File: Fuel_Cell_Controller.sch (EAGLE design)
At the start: 27 parts, among them U1 MAX232PTH

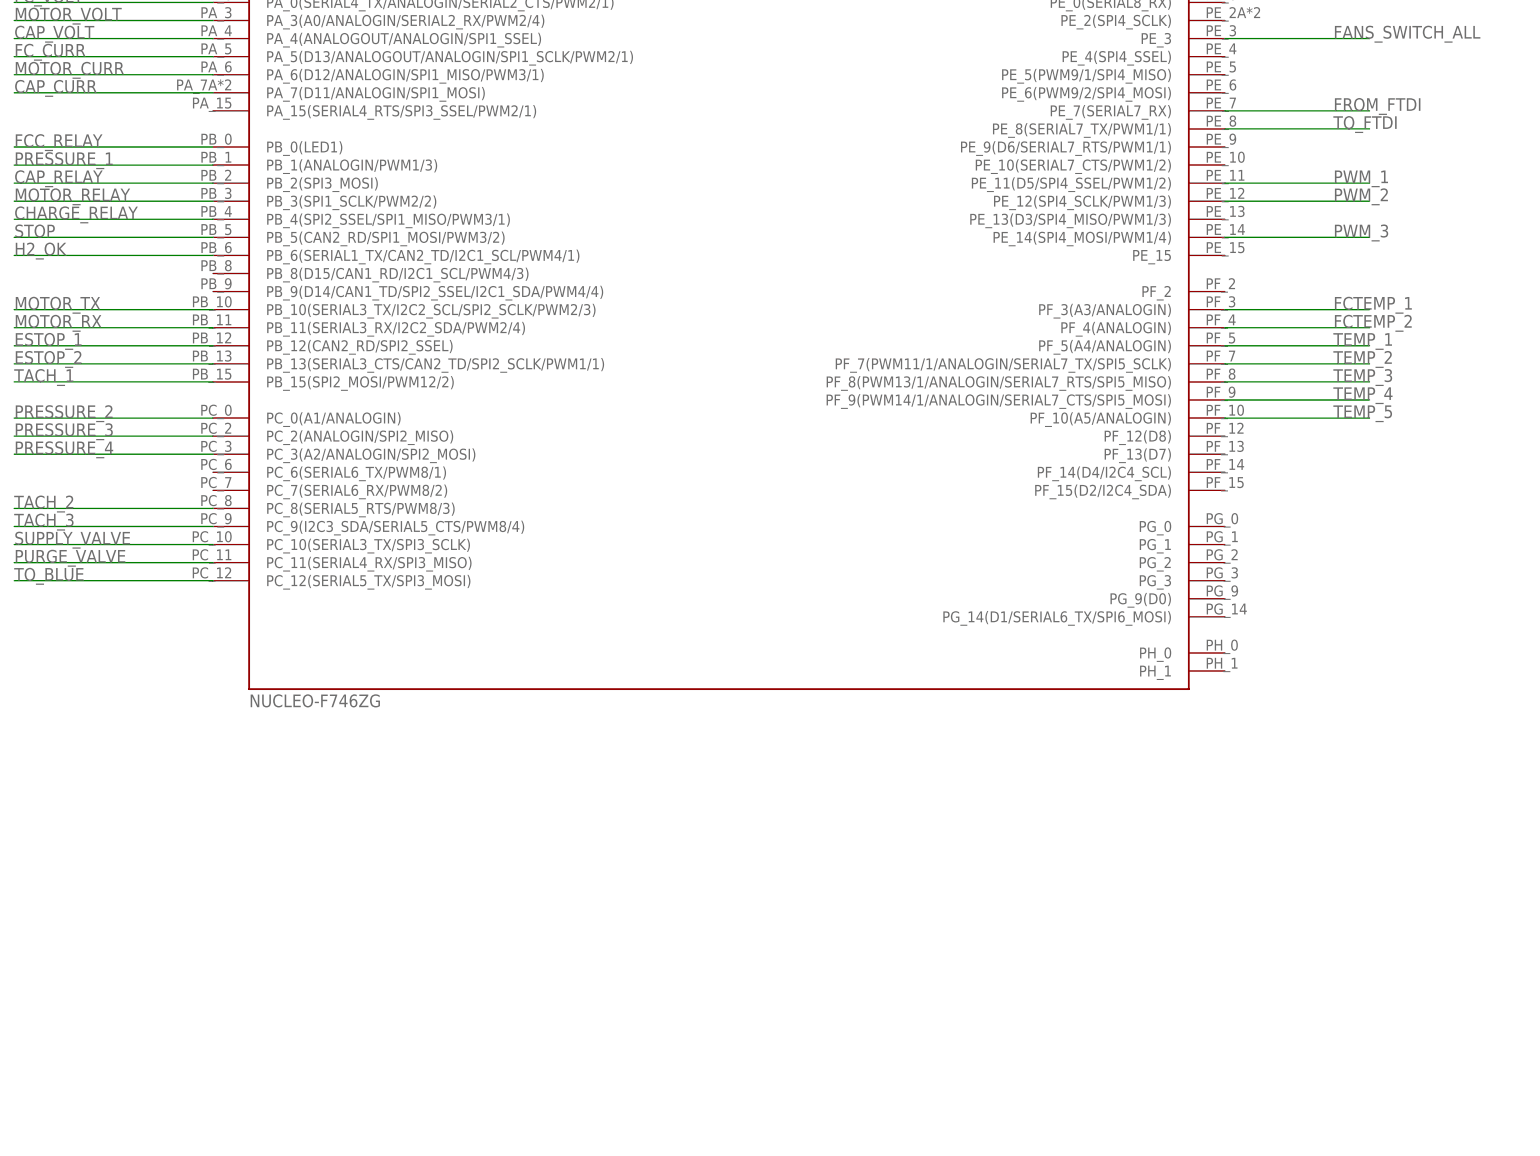
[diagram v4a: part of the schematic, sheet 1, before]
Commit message: added some buffers
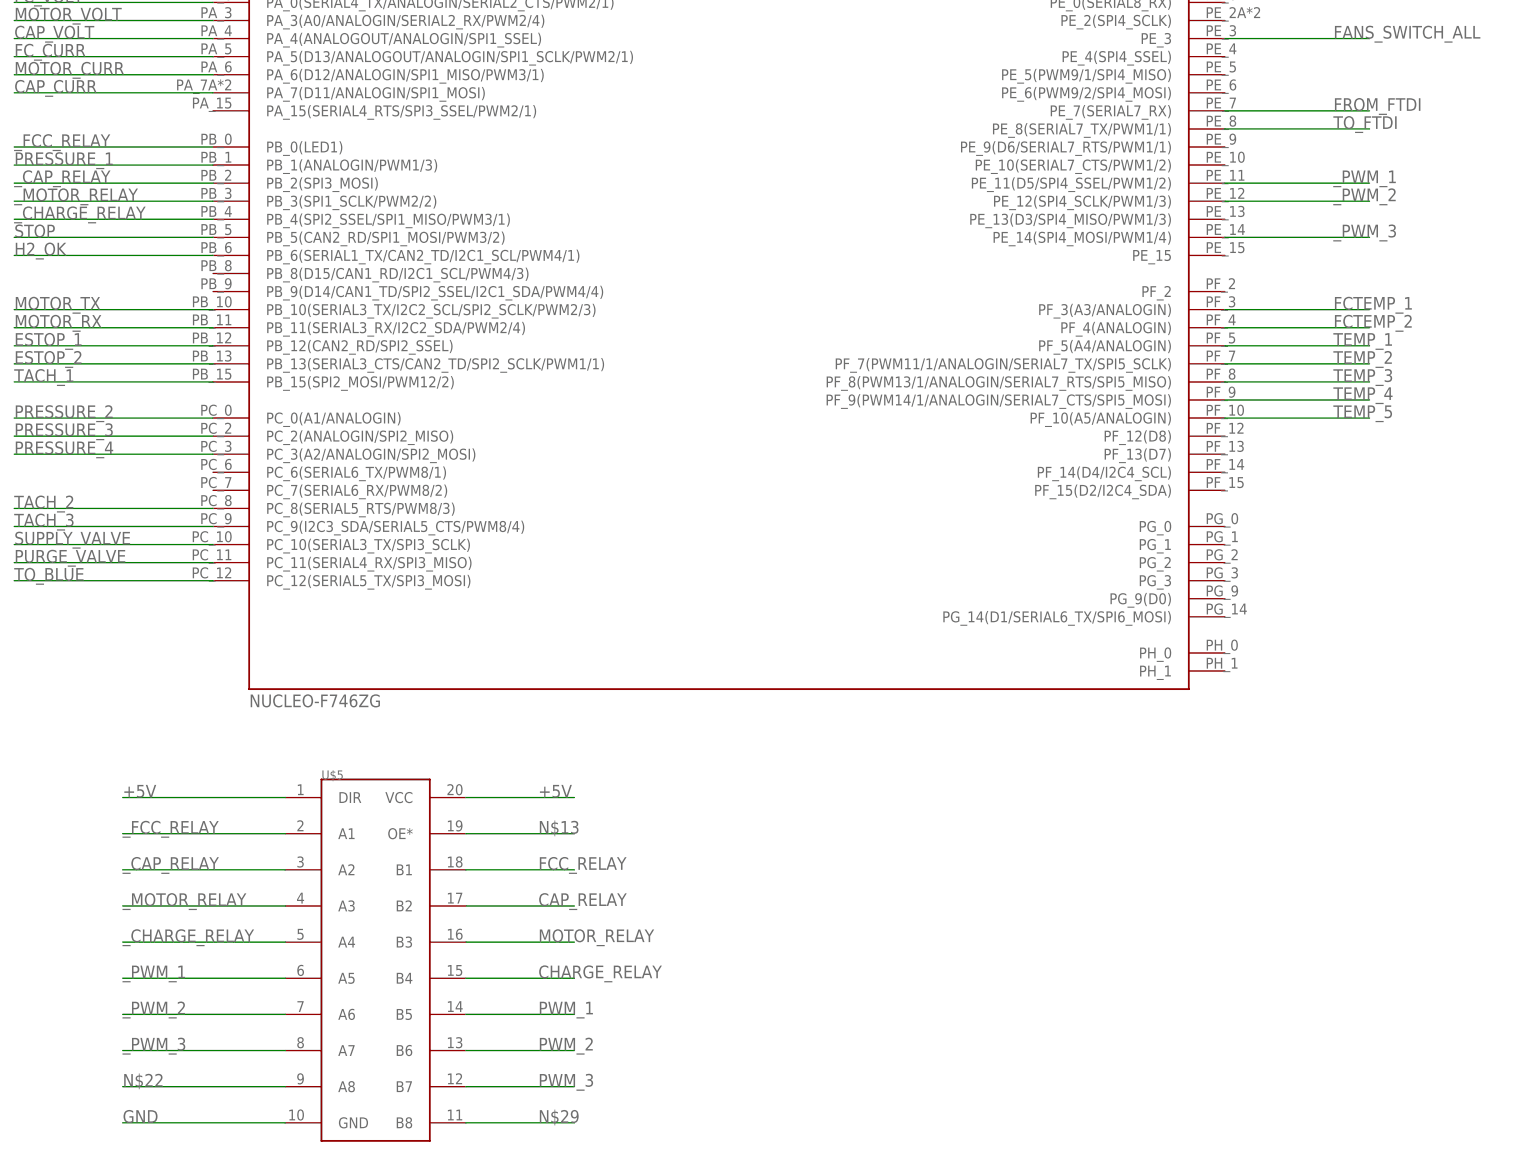
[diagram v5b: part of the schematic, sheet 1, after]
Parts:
- added U$5: SN74LVC245AN, FCC_parts:SN74LVC245AN
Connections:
- new net N$13: U$5.OE*
- new net N$22: U$5.A8
- new net N$29: U$5.B8
- new net _CAP_RELAY: U$1.PB_2(SPI3_MOSI), U$5.A2
- new net _CHARGE_RELAY: U$1.PB_4(SPI2_SSEL/SPI1_MISO/PWM3/1), U$5.A4
- new net _FCC_RELAY: U$1.PB_0(LED1), U$5.A1
- new net _MOTOR_RELAY: U$1.PB_3(SPI1_SCLK/PWM2/2), U$5.A3
- new net _PWM_1: U$1.PE_11(D5/SPI4_SSEL/PWM1/2), U$5.A5
- new net _PWM_2: U$1.PE_12(SPI4_SCLK/PWM1/3), U$5.A6
- new net _PWM_3: U$1.PE_14(SPI4_MOSI/PWM1/4), U$5.A7
- net +5V: now also U$5.DIR, U$5.VCC
- net CAP_RELAY: now also U$5.B2; no longer U$1.PB_2(SPI3_MOSI)
- net CHARGE_RELAY: now also U$5.B4; no longer U$1.PB_4(SPI2_SSEL/SPI1_MISO/PWM3/1)
- net FCC_RELAY: now also U$5.B1; no longer U$1.PB_0(LED1)
- net GND: now also U$5.GND
- net MOTOR_RELAY: now also U$5.B3; no longer U$1.PB_3(SPI1_SCLK/PWM2/2)
- net PWM_1: now also U$5.B5; no longer U$1.PE_11(D5/SPI4_SSEL/PWM1/2)
- net PWM_2: now also U$5.B6; no longer U$1.PE_12(SPI4_SCLK/PWM1/3)
- net PWM_3: now also U$5.B7; no longer U$1.PE_14(SPI4_MOSI/PWM1/4)

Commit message: buffer changes
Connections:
- removed net N$13: U$5.OE*
- removed net N$22: U$5.A8
- removed net N$29: U$5.B8
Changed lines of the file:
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@@
-</segment>
-</net>
-<net name="N$13" class="0">
-<segment>
-<pinref part="U$5" gate="G$1" pin="OE*"/>
-<wire x1="-35.56" y1="-88.9" x2="-20.32" y2="-88.9" width="0.1524" layer="91"/>
-<label x="-25.4" y="-88.9" size="1.778" layer="95"/>
 </segment>
 </net>
@@
 <wire x1="-35.56" y1="-93.98" x2="-20.32" y2="-93.98" width="0.1524" layer="91"/>
 <label x="-25.4" y="-93.98" size="1.778" layer="95"/>
-</segment>
-</net>
-<net name="N$22" class="0">
-<segment>
-<pinref part="U$5" gate="G$1" pin="A8"/>
-<wire x1="-60.96" y1="-124.46" x2="-83.82" y2="-124.46" width="0.1524" layer="91"/>
-<label x="-83.82" y="-124.46" size="1.778" layer="95"/>
 </segment>
 </net>
@@
 </segment>
 </net>
-<net name="N$29" class="0">
-<segment>
-<pinref part="U$5" gate="G$1" pin="B8"/>
-<wire x1="-35.56" y1="-129.54" x2="-20.32" y2="-129.54" width="0.1524" layer="91"/>
-<label x="-25.4" y="-129.54" size="1.778" layer="95"/>
-</segment>
-</net>

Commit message: Added humidity sensor
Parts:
- added JP1: (no value), jumper:JP2E
- added SHTSENSOR: SHT31-DIS, FCC_parts:SHT31-DIS
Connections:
- new net HUMID_RESET: U$1.PC_6(SERIAL6_TX/PWM8/1)
- new net HUMID_RST: SHTSENSOR.RST
- new net I2C1_SCL: U$1.PB_8(D15/CAN1_RD/I2C1_SCL/PWM4/3)
- new net ISC1_SCL: SHTSENSOR.SCL
- new net ISC1_SDA: SHTSENSOR.SDA, U$1.PB_9(D14/CAN1_TD/SPI2_SSEL/I2C1_SDA/PWM4/4)
- new net SHT_ADR: JP1.2, SHTSENSOR.ADR
- net +5V: now also JP1.3, SHTSENSOR.VIN
- net GND: now also JP1.1, SHTSENSOR.GND
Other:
- note added: "TEMP/HUMID SENSOR"
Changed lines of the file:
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@@
 <part name="U$10" library="FCC_parts" deviceset="UMFT234XF" device="UMFT234XF"/>
 <part name="U$5" library="FCC_parts" deviceset="SN74LVC245AN" device=""/>
+<part name="SHTSENSOR" library="FCC_parts" deviceset="SHT31-DIS" device=""/>
+<part name="JP1" library="jumper" library_urn="urn:adsk.eagle:library:252" deviceset="JP2E" device="" package3d_urn="urn:adsk.eagle:package:15452/1"/>
 </parts>
 <sheets>
@@
 <wire x1="281.94" y1="33.02" x2="281.94" y2="-15.24" width="0.1524" layer="94"/>
 <wire x1="281.94" y1="-15.24" x2="210.82" y2="-15.24" width="0.1524" layer="94"/>
+<text x="228.6" y="-25.4" size="3.81" layer="94">TEMP/HUMID SENSOR</text>
+<wire x1="210.82" y1="-96.52" x2="304.8" y2="-96.52" width="0.1524" layer="94"/>
+<wire x1="304.8" y1="-96.52" x2="304.8" y2="-15.24" width="0.1524" layer="94"/>
+<wire x1="304.8" y1="-15.24" x2="281.94" y2="-15.24" width="0.1524" layer="94"/>
 </plain>
 <instances>
@@
 <instance part="U$10" gate="G$1" x="220.98" y="53.34"/>
 <instance part="U$5" gate="G$1" x="-48.26" y="-106.68"/>
+<instance part="SHTSENSOR" gate="G$1" x="266.7" y="-58.42"/>
+<instance part="JP1" gate="1" x="248.92" y="-86.36" rot="R90"/>
 </instances>
 <busses>
@@
 <wire x1="-60.96" y1="-129.54" x2="-83.82" y2="-129.54" width="0.1524" layer="91"/>
 <label x="-83.82" y="-129.54" size="1.778" layer="95"/>
+</segment>
+<segment>
+<pinref part="SHTSENSOR" gate="G$1" pin="GND"/>
+<wire x1="254" y1="-48.26" x2="236.22" y2="-48.26" width="0.1524" layer="91"/>
+<label x="236.22" y="-48.26" size="1.778" layer="95"/>
+</segment>
+<segment>
+<pinref part="JP1" gate="1" pin="1"/>
+<wire x1="251.46" y1="-88.9" x2="254" y2="-88.9" width="0.1524" layer="91"/>
+<wire x1="254" y1="-88.9" x2="254" y2="-91.44" width="0.1524" layer="91"/>
+<label x="254" y="-88.9" size="1.778" layer="95" rot="R270"/>
 </segment>
 </net>
@@
 <label x="-25.4" y="-83.82" size="1.778" layer="95"/>
 </segment>
+<segment>
+<pinref part="SHTSENSOR" gate="G$1" pin="VIN"/>
+<wire x1="254" y1="-43.18" x2="236.22" y2="-43.18" width="0.1524" layer="91"/>
+<label x="236.22" y="-43.18" size="1.778" layer="95"/>
+</segment>
+<segment>
+<pinref part="JP1" gate="1" pin="3"/>
+<wire x1="251.46" y1="-83.82" x2="254" y2="-83.82" width="0.1524" layer="91"/>
+<wire x1="254" y1="-83.82" x2="254" y2="-81.28" width="0.1524" layer="91"/>
+<label x="254" y="-78.74" size="1.778" layer="95" rot="R270"/>
+</segment>
 </net>
 <net name="FROM_OPEN" class="0">
@@
 <wire x1="-60.96" y1="-119.38" x2="-83.82" y2="-119.38" width="0.1524" layer="91"/>
 <label x="-83.82" y="-119.38" size="1.778" layer="95"/>
+</segment>
+</net>
+<net name="ISC1_SCL" class="0">
+<segment>
+<pinref part="SHTSENSOR" gate="G$1" pin="SCL"/>
+<wire x1="254" y1="-53.34" x2="236.22" y2="-53.34" width="0.1524" layer="91"/>
+<label x="236.22" y="-53.34" size="1.778" layer="95"/>
+</segment>
+</net>
+<net name="SHT_ADR" class="0">
+<segment>
+<pinref part="SHTSENSOR" gate="G$1" pin="ADR"/>
+<wire x1="254" y1="-63.5" x2="236.22" y2="-63.5" width="0.1524" layer="91"/>
+<label x="236.22" y="-63.5" size="1.778" layer="95"/>
+</segment>
+<segment>
+<pinref part="JP1" gate="1" pin="2"/>
+<wire x1="251.46" y1="-86.36" x2="274.32" y2="-86.36" width="0.1524" layer="91"/>
+<label x="264.16" y="-86.36" size="1.778" layer="95"/>
+</segment>
+</net>
+<net name="HUMID_RST" class="0">
+<segment>
+<pinref part="SHTSENSOR" gate="G$1" pin="RST"/>
+<wire x1="254" y1="-68.58" x2="236.22" y2="-68.58" width="0.1524" layer="91"/>
+<label x="236.22" y="-68.58" size="1.778" layer="95"/>
+</segment>
+</net>
+<net name="I2C1_SCL" class="0">
+<segment>
+<pinref part="U$1" gate="G$1" pin="PB_8(D15/CAN1_RD/I2C1_SCL/PWM4/3)"/>
+<wire x1="-71.12" y1="-10.16" x2="-99.06" y2="-10.16" width="0.1524" layer="91"/>
+<label x="-99.06" y="-10.16" size="1.778" layer="95"/>
+</segment>
+</net>
+<net name="ISC1_SDA" class="0">
+<segment>
+<pinref part="U$1" gate="G$1" pin="PB_9(D14/CAN1_TD/SPI2_SSEL/I2C1_SDA/PWM4/4)"/>
+<wire x1="-71.12" y1="-12.7" x2="-99.06" y2="-12.7" width="0.1524" layer="91"/>
+<label x="-99.06" y="-12.7" size="1.778" layer="95"/>
+</segment>
+<segment>
+<pinref part="SHTSENSOR" gate="G$1" pin="SDA"/>
+<wire x1="254" y1="-58.42" x2="236.22" y2="-58.42" width="0.1524" layer="91"/>
+<label x="236.22" y="-58.42" size="1.778" layer="95"/>
+</segment>
+</net>
+<net name="HUMID_RESET" class="0">
+<segment>
+<pinref part="U$1" gate="G$1" pin="PC_6(SERIAL6_TX/PWM8/1)"/>
+<wire x1="-71.12" y1="-38.1" x2="-99.06" y2="-38.1" width="0.1524" layer="91"/>
+<label x="-99.06" y="-38.1" size="1.778" layer="95"/>
 </segment>
 </net>
@@
 </drawing>
 <compatibility>
+<note version="6.3" minversion="6.2.2" severity="warning">
+Since Version 6.2.2 text objects can contain more than one line,
+which will not be processed correctly with this version.
+</note>
 <note version="8.2" severity="warning">
 Since Version 8.2, EAGLE supports online libraries. The ids
